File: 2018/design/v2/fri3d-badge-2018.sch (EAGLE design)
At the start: 125 parts

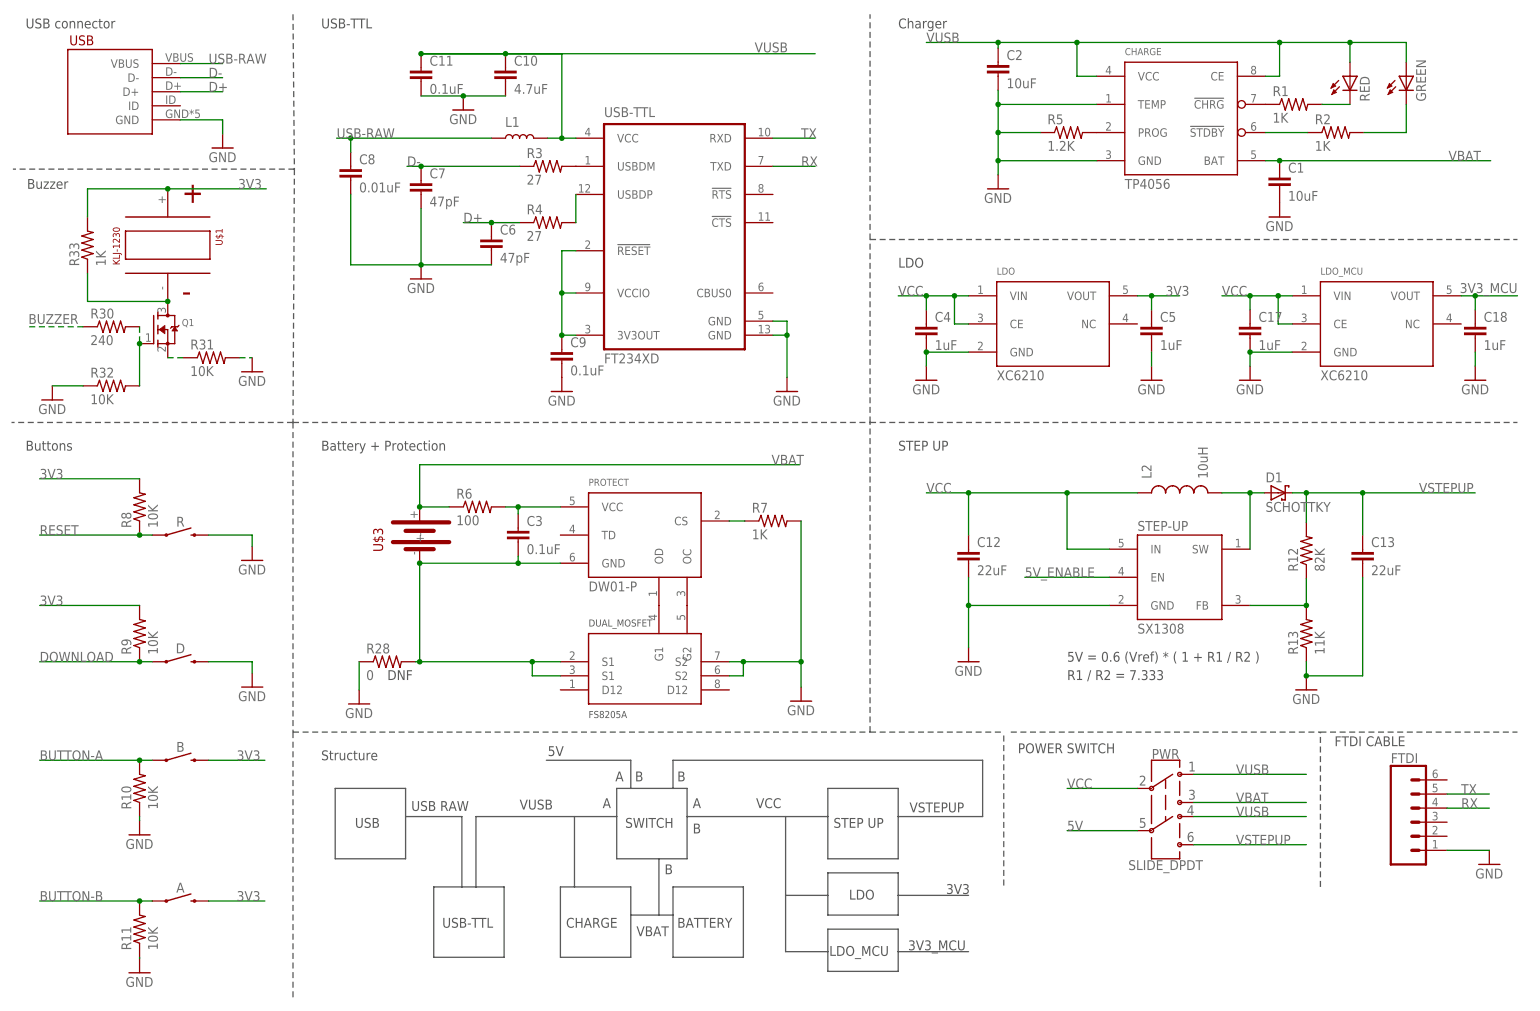
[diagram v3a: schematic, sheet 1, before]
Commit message: changed step-up inductor + testpoints/shortcuts
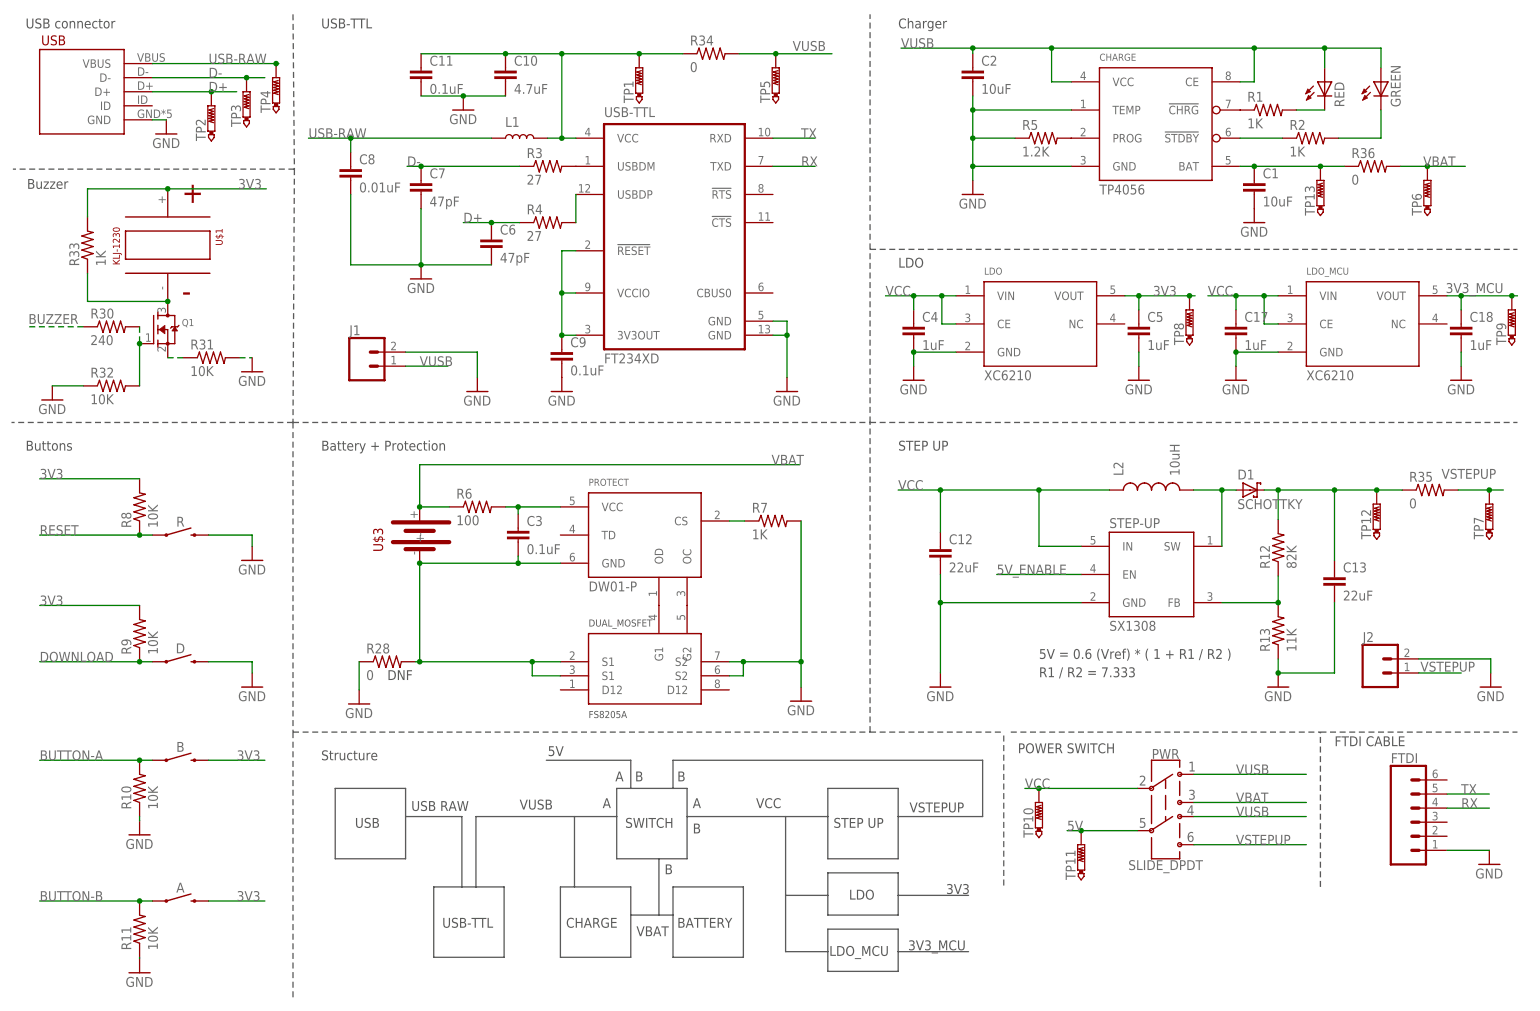
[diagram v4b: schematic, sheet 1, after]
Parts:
- added J1, J2: (no value), SparkFun-Connectors:CONN_02
- added R34, R35, R36: 0, passive:RESISTOR0805-RES
- added TP1, TP10, TP11, TP12, TP13, TP2, TP3, TP4, TP5, TP6, TP7, TP8, TP9: PTR1B1,27, testpad:PTR1B1,27
- L2: device passive:INDUCTOR0805 -> passive:TYS6045100M-10
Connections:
- new net N$1: C13.1, D1.C, R12.2, R35.1, TP12.TP
- new net N$22: C1.1, CHARGE.BAT, R36.1, TP13.TP
- new net USB-FILTERED: C10.1, C11.1, L1.2, R34.1, TP1.TP, USB-TTL.VCC
- net 3V3: now also TP8.TP
- net 3V3_MCU: now also TP9.TP
- net 5V: now also TP11.TP
- net D+: now also TP2.TP
- net D-: now also TP3.TP
- net GND: now also J1.2, J2.2
- net USB-RAW: now also TP4.TP
- net VBAT: now also R36.2, TP6.TP; no longer C1.1, CHARGE.BAT
- net VCC: now also TP10.TP
- net VSTEPUP: now also J2.1, R35.2, TP7.TP; no longer C13.1, D1.C, R12.2
- net VUSB: now also J1.1, R34.2, TP5.TP; no longer C10.1, C11.1, L1.2, USB-TTL.VCC
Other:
- moved on the sheet: C1, C12, C13, C17, C18, C2, C4, C5, CHARGE, D1, GREEN, L2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

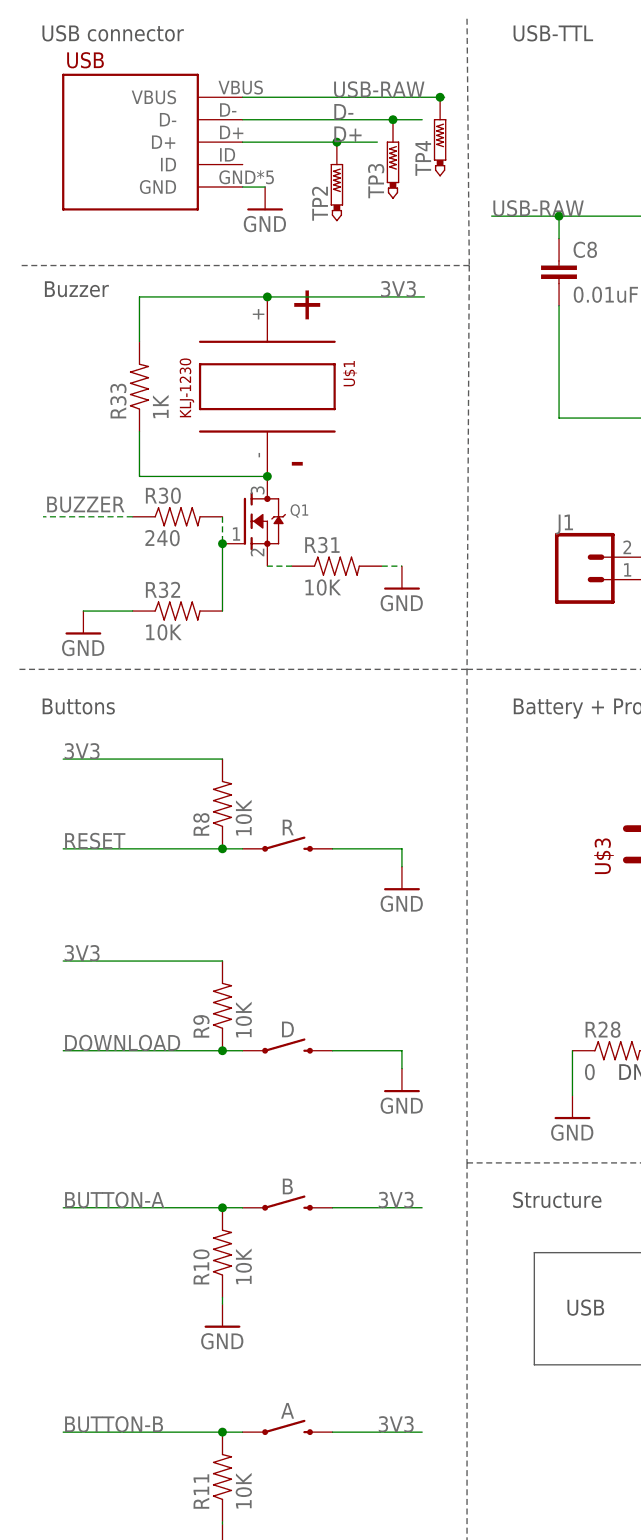
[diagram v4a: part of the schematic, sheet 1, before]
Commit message: fixed USB GND/SHIELD issue
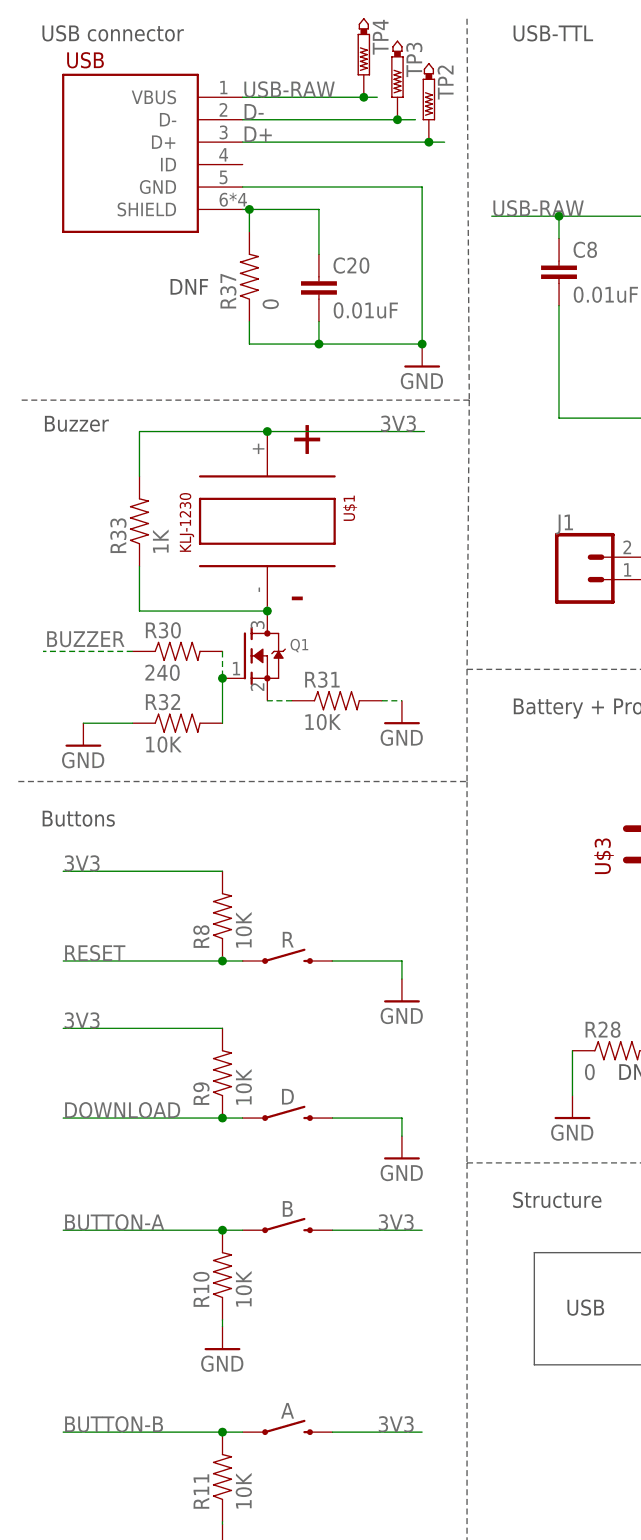
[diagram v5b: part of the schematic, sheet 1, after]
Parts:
- added C20: 0.01uF, passive:CAP0805
- added R37: 0, passive:RESISTOR0805-RES
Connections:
- new net N$23: C20.1, R37.2, USB.SHIELD
- net GND: now also C20.2, R37.1
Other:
- moved on the sheet: B, D, Q1, R, R10, R30, R31, R32, R33, R8, R9, TP2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

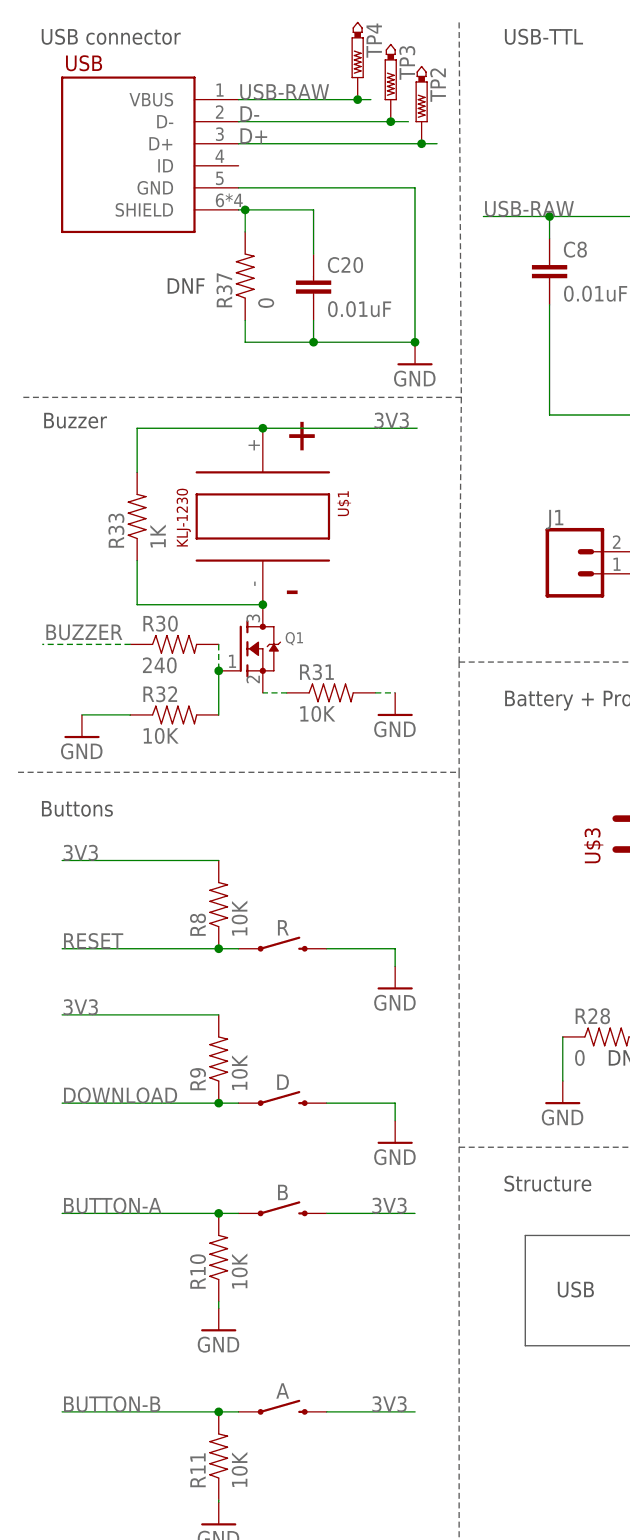
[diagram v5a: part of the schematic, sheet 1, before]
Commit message: added ESD protection, enlarged power planes/traces
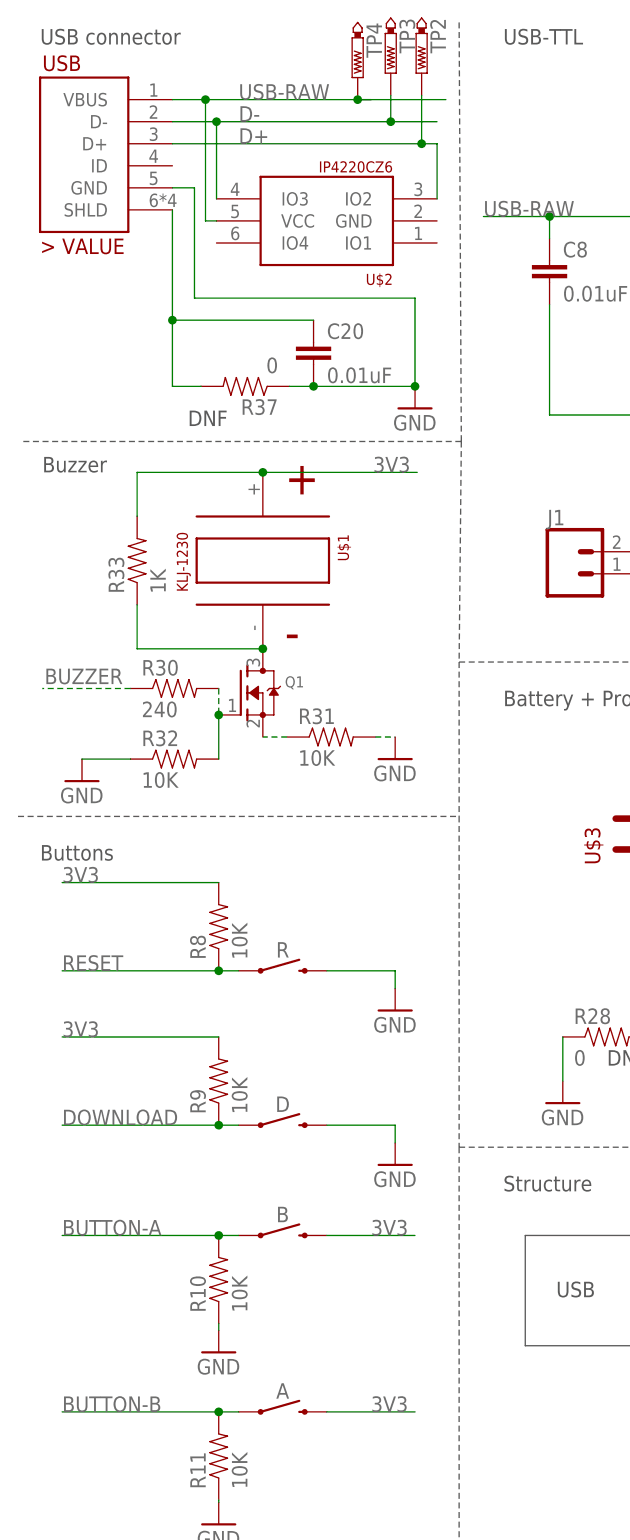
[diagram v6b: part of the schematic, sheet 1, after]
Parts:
- removed BDG: (no value), SparkFun-Connectors:CONN_03
- removed C14, C15, C16: 0.1uF, passive:CAP0805
- removed R29: 0, passive:RESISTOR0805-RES
- removed WS1, WS2, WS3: WS2812B5050, adafruit:WS2812B5050
- added U$2: IP4220CZ6, ic:IP4220CZ6
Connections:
- removed net EXP_5V: C14.1, C15.1, C16.1, R29.2, WS1.VDD, WS2.VDD, WS3.VDD
- removed net EXP_GND: BDG.1, C14.2, C15.2, C16.2, WS1.GND, WS2.GND, WS3.GND
- removed net N$16: BDG.2, R29.1
- removed net N$17: WS1.DO, WS2.DI
- removed net N$60: WS2.DO, WS3.DI
- removed net N$61: BDG.3, WS1.DI
- net D+: now also U$2.IO2
- net D-: now also U$2.IO3
- net N$23: now also USB.SHLD; no longer USB.SHIELD
- net USB-RAW: now also U$2.VCC
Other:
- note removed: "0Ohm or diode"
- note removed: "EXPANSION BOARD"
- moved on the sheet: B, C20, D, Q1, R, R10, R30, R31, R32, R33, R37, R8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
